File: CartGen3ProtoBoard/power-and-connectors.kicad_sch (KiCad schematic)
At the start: 2 parts, among them J1 Conn_01x02_Male

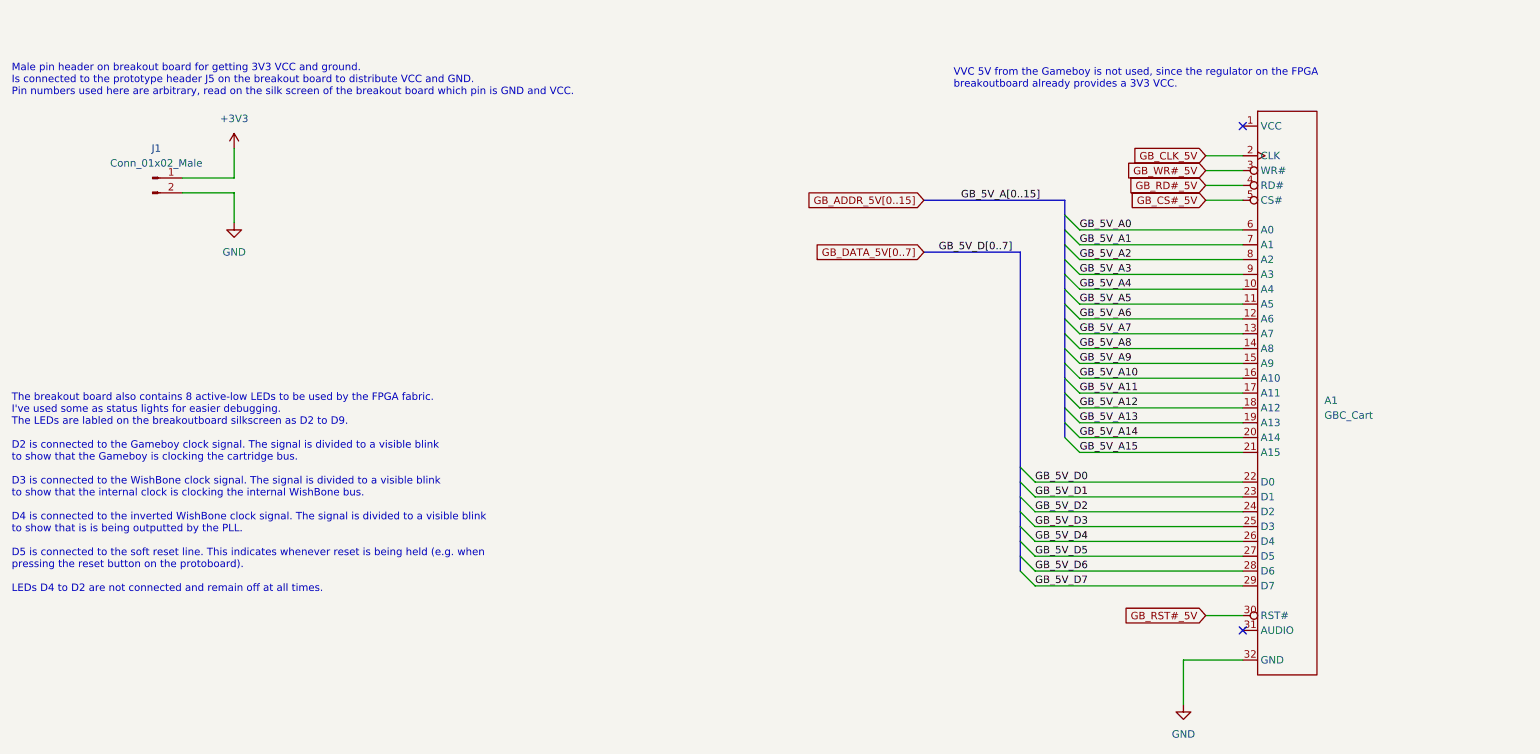
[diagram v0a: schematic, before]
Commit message: Added audio schematic
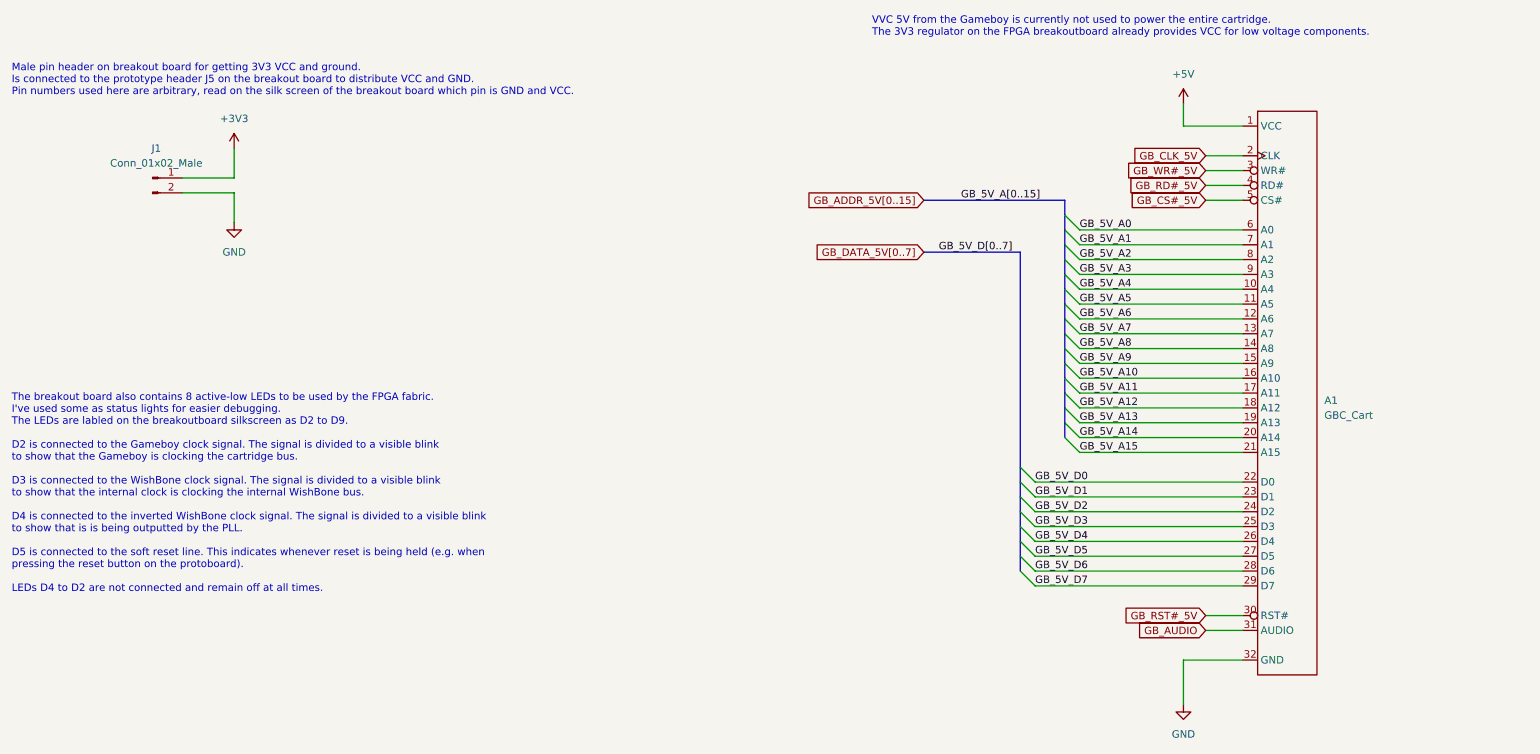
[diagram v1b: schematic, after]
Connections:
- net +5V: now reaches A1.1 (VCC)
- net GB_AUDIO: now reaches A1.31 (AUDIO)
- no-connect marks 2 -> 0
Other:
- note added: "VVC 5V from the Gameboy is currently not used to power the entire cartridge. The 3V3 regulator on the FPGA breakoutboard already provides VCC for low voltage components."
- note removed: "VVC 5V from the Gameboy is not used, since the regulator on the FPGA breakoutboard already provides a 3V3 VCC."
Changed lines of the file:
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@@
     (title "Power and connectors")
   )
-  (no_connect (at 242.57 43.18))
-  (no_connect (at 242.57 129.54))
   (bus_entry (at 212.09 68.58) (size 2.54 2.54)
     (stroke (width 0) (type default) (color 0 0 0 0))
@@
     (stroke (width 0) (type default) (color 0 0 0 0))
   )
+  (wire (pts (xy 232.41 43.18) (xy 242.57 43.18))
+    (stroke (width 0) (type default) (color 0 0 0 0))
+  )
   (wire (pts (xy 214.63 63.5) (xy 242.57 63.5))
     (stroke (width 0) (type default) (color 0 0 0 0))
@@
     (stroke (width 0) (type default) (color 0 0 0 0))
   )
+  (wire (pts (xy 236.22 129.54) (xy 242.57 129.54))
+    (stroke (width 0) (type default) (color 0 0 0 0))
+  )
   (wire (pts (xy 214.63 81.28) (xy 242.57 81.28))
     (stroke (width 0) (type default) (color 0 0 0 0))
@@
   )
   (bus (pts (xy 212.09 88.9) (xy 212.09 86.36))
+    (stroke (width 0) (type default) (color 0 0 0 0))
+  )
+  (wire (pts (xy 232.41 43.18) (xy 232.41 39.37))
     (stroke (width 0) (type default) (color 0 0 0 0))
   )
@@
     (effects (font (size 1.27 1.27)) (justify left bottom))
   )
-  (text "VVC 5V from the Gameboy is not used, since the regulator on the FPGA\nbreakoutboard already provides a 3V3 VCC."
-    (at 193.04 36.83 0)
+  (text "VVC 5V from the Gameboy is currently not used to power the entire cartridge.\nThe 3V3 regulator on the FPGA breakoutboard already provides VCC for low voltage components."
+    (at 179.07 27.94 0)
     (effects (font (size 1.27 1.27)) (justify left bottom))
   )
@@
     (effects (font (size 1.27 1.27)) (justify right))
     (property "Intersheet References" "${INTERSHEET_REFS}" (id 0) (at 222.3164 126.9206 0)
+      (effects (font (size 1.27 1.27)) (justify right) hide)
+    )
+  )
+  (global_label "GB_AUDIO" (shape input) (at 236.22 129.54 180) (fields_autoplaced)
+    (effects (font (size 1.27 1.27)) (justify right))
+    (property "Intersheet References" "${INTERSHEET_REFS}" (id 0) (at 224.675 129.4606 0)
       (effects (font (size 1.27 1.27)) (justify right) hide)
     )
@@
       (effects (font (size 1.27 1.27)) hide)
     )
+    (pin "1")
+  )
+  (symbol (lib_id "power:+5V") (at 232.41 39.37 0) (unit 1)
+    (in_bom yes) (on_board yes) (fields_autoplaced)
+    (property "Reference" "#PWR?" (id 0) (at 232.41 43.18 0)
+      (effects (font (size 1.27 1.27)) hide)
+    )
+    (property "Value" "+5V" (id 1) (at 232.41 34.29 0))
+    (property "Footprint" "" (id 2) (at 232.41 39.37 0)
+      (effects (font (size 1.27 1.27)) hide)
+    )
+    (property "Datasheet" "" (id 3) (at 232.41 39.37 0)
+      (effects (font (size 1.27 1.27)) hide)
+    )
